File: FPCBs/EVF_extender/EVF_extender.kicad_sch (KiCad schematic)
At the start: 2 parts, among them J3 FR02C061JA1-R5000, J4 FPC_2Rows-61Pins_0.2mm

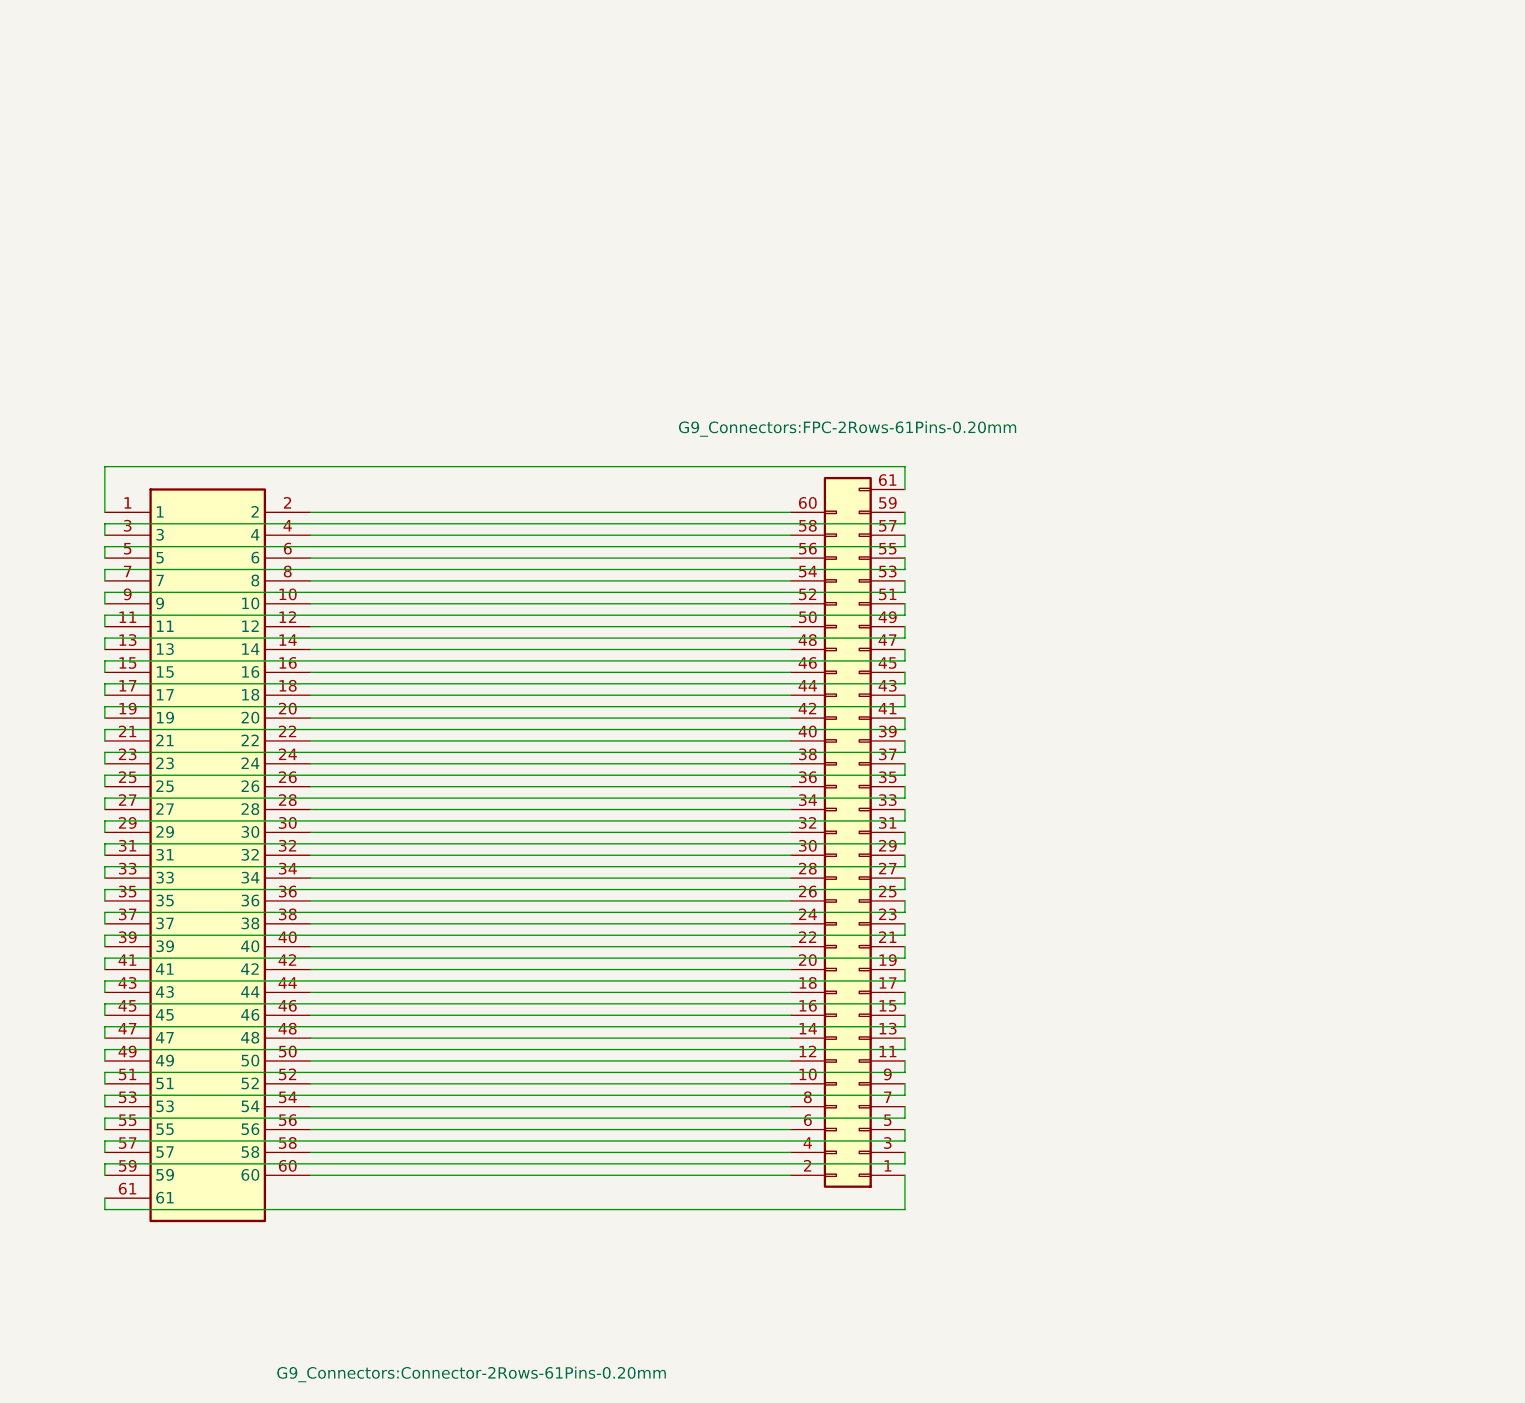
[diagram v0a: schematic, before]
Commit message: Add EVF extender FPCB
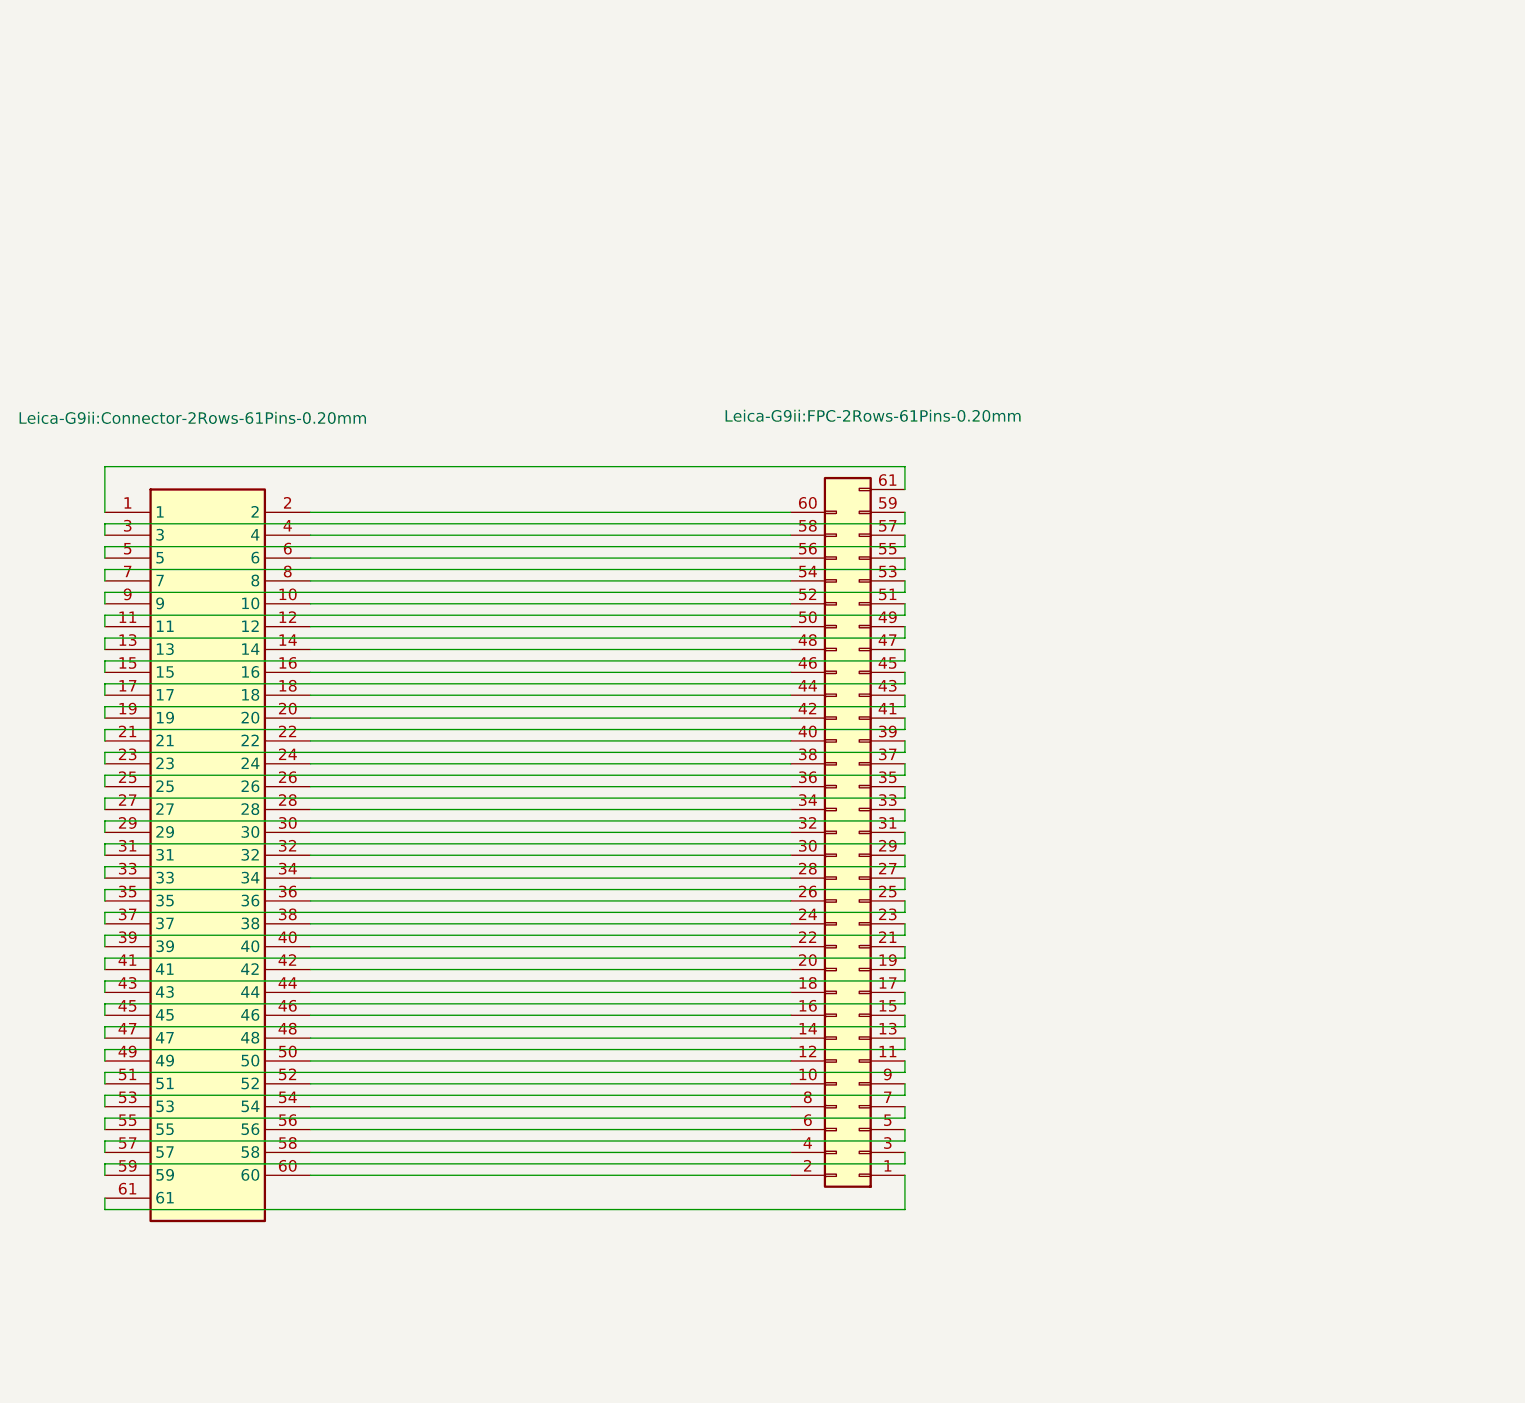
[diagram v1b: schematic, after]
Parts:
- J3: footprint G9_Connectors:Connector-2Rows-61Pins-0.20mm -> Leica-G9ii:Connector-2Rows-61Pins-0.20mm
- J4: footprint G9_Connectors:FPC-2Rows-61Pins-0.20mm -> Leica-G9ii:FPC-2Rows-61Pins-0.20mm
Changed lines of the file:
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@@
 (kicad_sch
-	(version 20231120)
+	(version 20250114)
 	(generator "eeschema")
-	(generator_version "8.0")
+	(generator_version "9.0")
 	(paper "A4")
 	(wire
@@
 		(on_board yes)
 		(dnp no)
-		(fields_autoplaced yes)
 		(property "Reference" "J3"
 			(at 48.26 90.17 0)
@@
 			)
 		)
-		(property "Footprint" "G9_Connectors:Connector-2Rows-61Pins-0.20mm"
-			(at 55.88 192.71 0)
+		(property "Footprint" "Leica-G9ii:Connector-2Rows-61Pins-0.20mm"
+			(at 27.178 86.614 0)
 			(effects
 				(font
@@
 			)
 		)
-		(property "Footprint" "G9_Connectors:FPC-2Rows-61Pins-0.20mm"
-			(at 119.38 88.392 0)
+		(property "Footprint" "Leica-G9ii:FPC-2Rows-61Pins-0.20mm"
+			(at 122.174 87.122 0)
 			(effects
 				(font
@@
 		)
 	)
+	(embedded_fonts no)
 )

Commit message: Correct evf distance
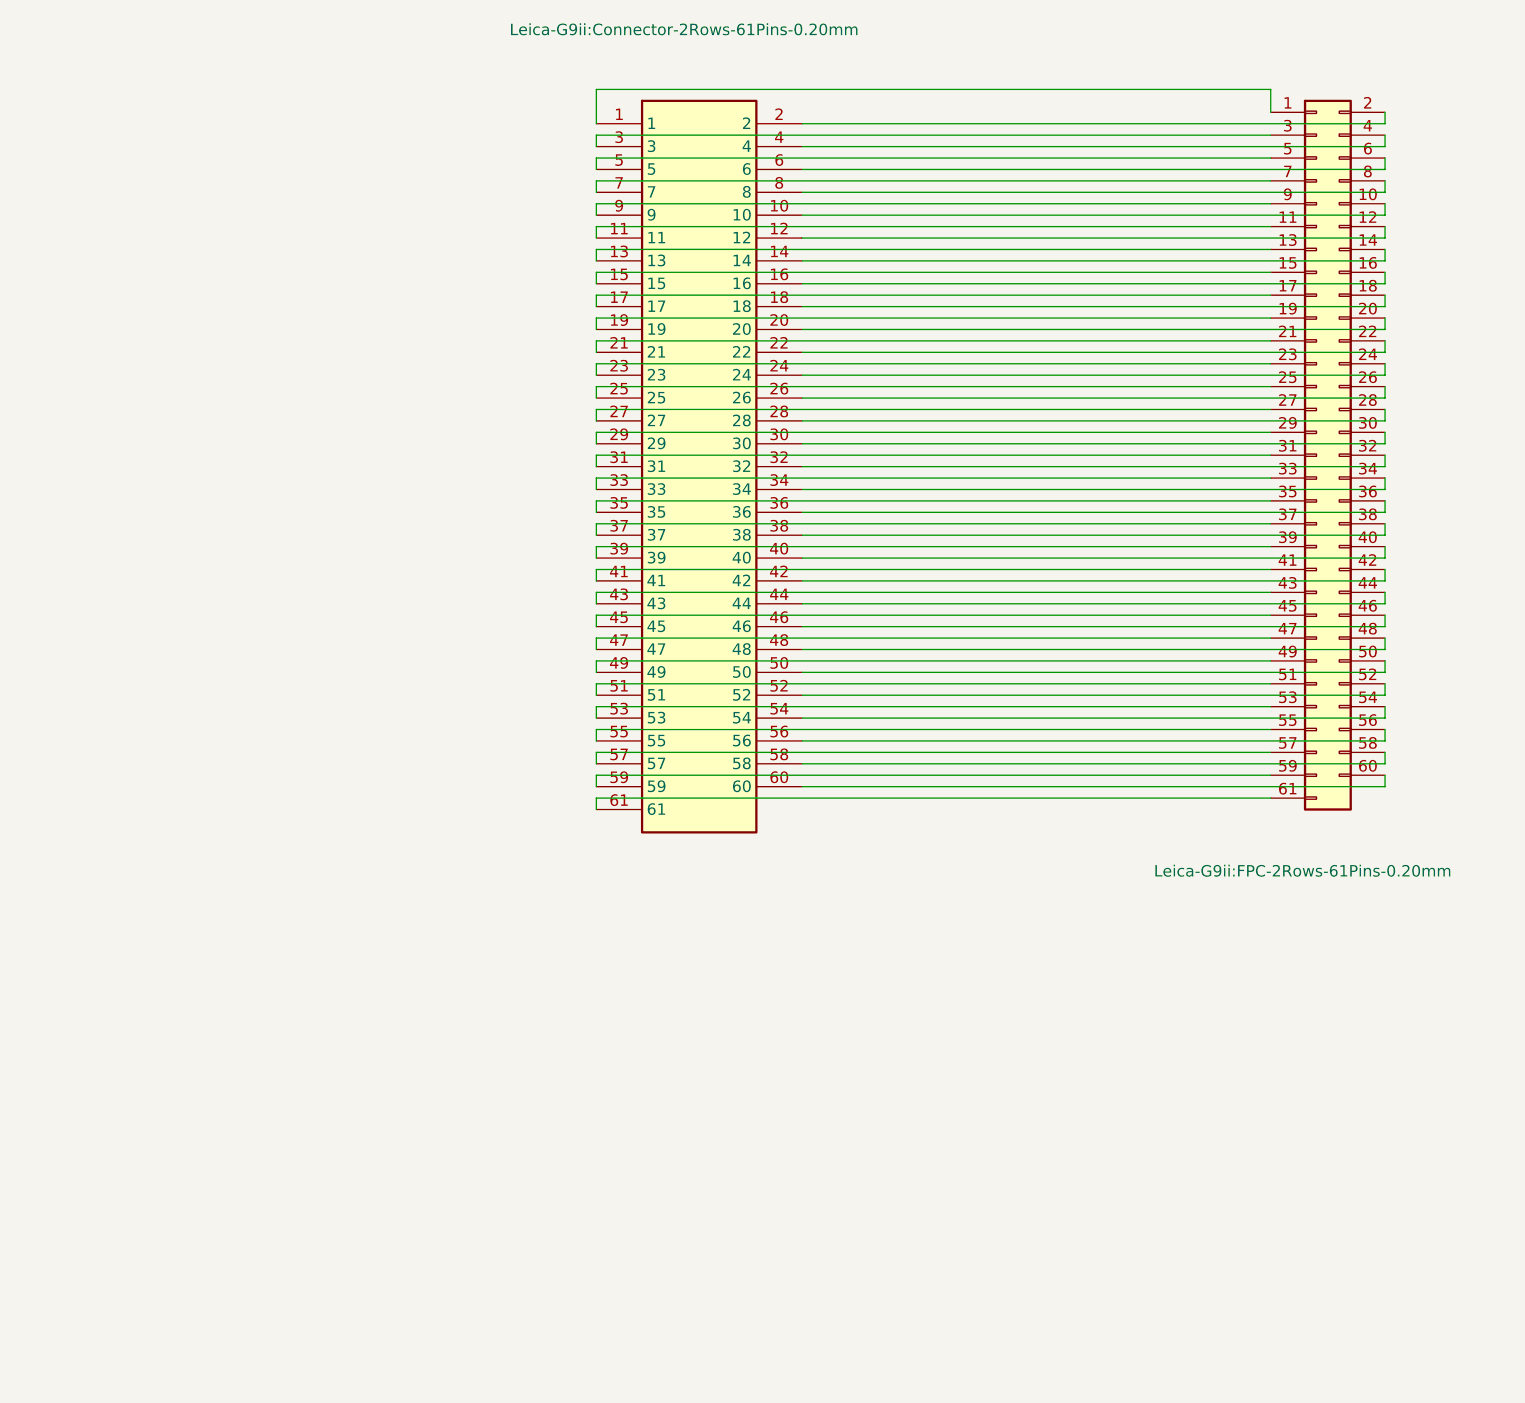
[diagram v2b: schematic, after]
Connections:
- net at J3.1: now also J4.1 (Pin_1); no longer J4.61 (Pin_61)
- net at J3.10: now also J4.10 (Pin_10); no longer J4.52 (Pin_52)
- net at J3.11: now also J4.11 (Pin_11); no longer J4.51 (Pin_51)
- net at J3.12: now also J4.12 (Pin_12); no longer J4.50 (Pin_50)
- net at J3.13: now also J4.13 (Pin_13); no longer J4.49 (Pin_49)
- net at J3.14: now also J4.14 (Pin_14); no longer J4.48 (Pin_48)
- net at J3.15: now also J4.15 (Pin_15); no longer J4.47 (Pin_47)
- net at J3.16: now also J4.16 (Pin_16); no longer J4.46 (Pin_46)
- net at J3.17: now also J4.17 (Pin_17); no longer J4.45 (Pin_45)
- net at J3.18: now also J4.18 (Pin_18); no longer J4.44 (Pin_44)
- net at J3.19: now also J4.19 (Pin_19); no longer J4.43 (Pin_43)
- net at J3.2: now also J4.2 (Pin_2); no longer J4.60 (Pin_60)
- net at J3.20: now also J4.20 (Pin_20); no longer J4.42 (Pin_42)
- net at J3.21: now also J4.21 (Pin_21); no longer J4.41 (Pin_41)
- net at J3.22: now also J4.22 (Pin_22); no longer J4.40 (Pin_40)
- net at J3.23: now also J4.23 (Pin_23); no longer J4.39 (Pin_39)
- net at J3.24: now also J4.24 (Pin_24); no longer J4.38 (Pin_38)
- net at J3.25: now also J4.25 (Pin_25); no longer J4.37 (Pin_37)
- net at J3.26: now also J4.26 (Pin_26); no longer J4.36 (Pin_36)
- net at J3.27: now also J4.27 (Pin_27); no longer J4.35 (Pin_35)
- net at J3.28: now also J4.28 (Pin_28); no longer J4.34 (Pin_34)
- net at J3.29: now also J4.29 (Pin_29); no longer J4.33 (Pin_33)
- net at J3.3: now also J4.3 (Pin_3); no longer J4.59 (Pin_59)
- net at J3.30: now also J4.30 (Pin_30); no longer J4.32 (Pin_32)
- net at J3.32: now also J4.32 (Pin_32); no longer J4.30 (Pin_30)
- net at J3.33: now also J4.33 (Pin_33); no longer J4.29 (Pin_29)
- net at J3.34: now also J4.34 (Pin_34); no longer J4.28 (Pin_28)
- net at J3.35: now also J4.35 (Pin_35); no longer J4.27 (Pin_27)
- net at J3.36: now also J4.36 (Pin_36); no longer J4.26 (Pin_26)
- net at J3.37: now also J4.37 (Pin_37); no longer J4.25 (Pin_25)
- net at J3.38: now also J4.38 (Pin_38); no longer J4.24 (Pin_24)
- net at J3.39: now also J4.39 (Pin_39); no longer J4.23 (Pin_23)
- net at J3.4: now also J4.4 (Pin_4); no longer J4.58 (Pin_58)
- net at J3.40: now also J4.40 (Pin_40); no longer J4.22 (Pin_22)
- net at J3.41: now also J4.41 (Pin_41); no longer J4.21 (Pin_21)
- net at J3.42: now also J4.42 (Pin_42); no longer J4.20 (Pin_20)
- net at J3.43: now also J4.43 (Pin_43); no longer J4.19 (Pin_19)
- net at J3.44: now also J4.44 (Pin_44); no longer J4.18 (Pin_18)
- net at J3.45: now also J4.45 (Pin_45); no longer J4.17 (Pin_17)
- net at J3.46: now also J4.46 (Pin_46); no longer J4.16 (Pin_16)
- net at J3.47: now also J4.47 (Pin_47); no longer J4.15 (Pin_15)
- net at J3.48: now also J4.48 (Pin_48); no longer J4.14 (Pin_14)
- net at J3.49: now also J4.49 (Pin_49); no longer J4.13 (Pin_13)
- net at J3.5: now also J4.5 (Pin_5); no longer J4.57 (Pin_57)
- net at J3.50: now also J4.50 (Pin_50); no longer J4.12 (Pin_12)
- net at J3.51: now also J4.51 (Pin_51); no longer J4.11 (Pin_11)
- net at J3.52: now also J4.52 (Pin_52); no longer J4.10 (Pin_10)
- net at J3.53: now also J4.53 (Pin_53); no longer J4.9 (Pin_9)
- net at J3.54: now also J4.54 (Pin_54); no longer J4.8 (Pin_8)
- net at J3.55: now also J4.55 (Pin_55); no longer J4.7 (Pin_7)
- net at J3.56: now also J4.56 (Pin_56); no longer J4.6 (Pin_6)
- net at J3.57: now also J4.57 (Pin_57); no longer J4.5 (Pin_5)
- net at J3.58: now also J4.58 (Pin_58); no longer J4.4 (Pin_4)
- net at J3.59: now also J4.59 (Pin_59); no longer J4.3 (Pin_3)
- net at J3.6: now also J4.6 (Pin_6); no longer J4.56 (Pin_56)
- net at J3.60: now also J4.60 (Pin_60); no longer J4.2 (Pin_2)
- net at J3.61: now also J4.61 (Pin_61); no longer J4.1 (Pin_1)
- net at J3.7: now also J4.7 (Pin_7); no longer J4.55 (Pin_55)
- net at J3.8: now also J4.8 (Pin_8); no longer J4.54 (Pin_54)
- net at J3.9: now also J4.9 (Pin_9); no longer J4.53 (Pin_53)
